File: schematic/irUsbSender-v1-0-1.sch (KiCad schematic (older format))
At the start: 38 parts, among them J1 USB_B_Micro, J2 Conn_01x06_Male, J3 Conn_01x03_Male, J4 Conn_01x02_Male, J5 Conn_01x02_Male, J6 Conn_01x02_Male, J7 Conn_01x08_Male, Q1 IRLML6344, U1 MCP1754-3302E_SOT89, U2 STM32F042K6Tx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

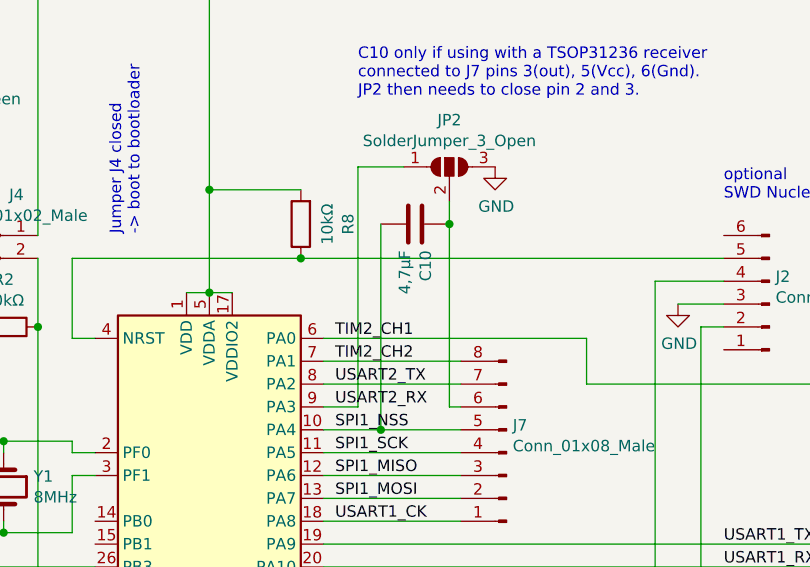
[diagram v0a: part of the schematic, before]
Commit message: Add build workflow. Add cnc milling. Improve doc. Minor fix in schematic. Minor improvement in host program.
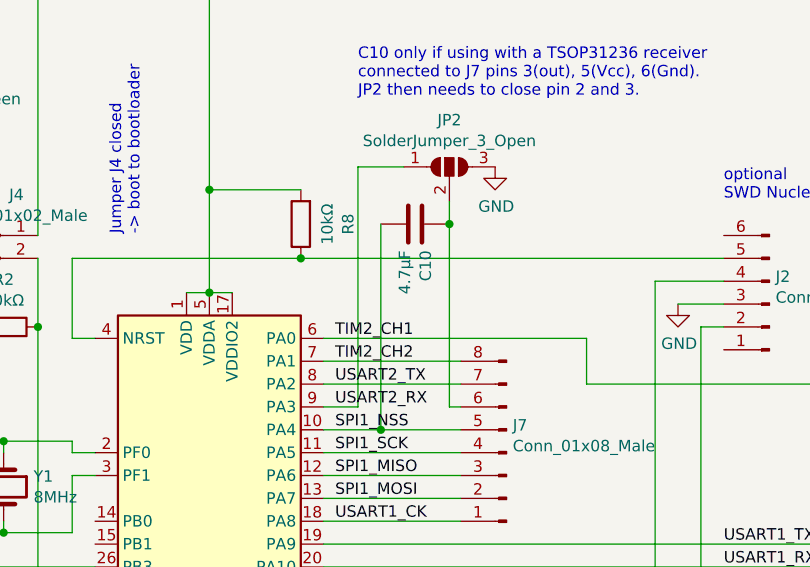
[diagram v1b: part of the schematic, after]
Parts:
- C10: value 4,7µF -> 4.7µF
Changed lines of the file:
@@
 Sheet 1 1
 Title "IRUSB"
-Date "2020-11-27"
+Date "2020-11-28"
 Rev "1.0.1"
 Comp "(c) 2020 by Malte Marwedel"
@@
 P 6500 2200
 F 0 "C10" H 6385 2154 50  0000 R CNN
-F 1 "4,7µF" H 6385 2245 50  0000 R CNN
+F 1 "4.7µF" H 6385 2245 50  0000 R CNN
 F 2 "Capacitor_SMD:C_0805_2012Metric_Pad1.15x1.40mm_HandSolder" H 6538 2050 50  0001 C CNN
 F 3 "~" H 6500 2200 50  0001 C CNN
